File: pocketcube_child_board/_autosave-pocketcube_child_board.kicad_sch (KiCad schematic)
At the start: 7 parts, among them J1 M55-7102042R, U1 SI3477DV-T1-GE3

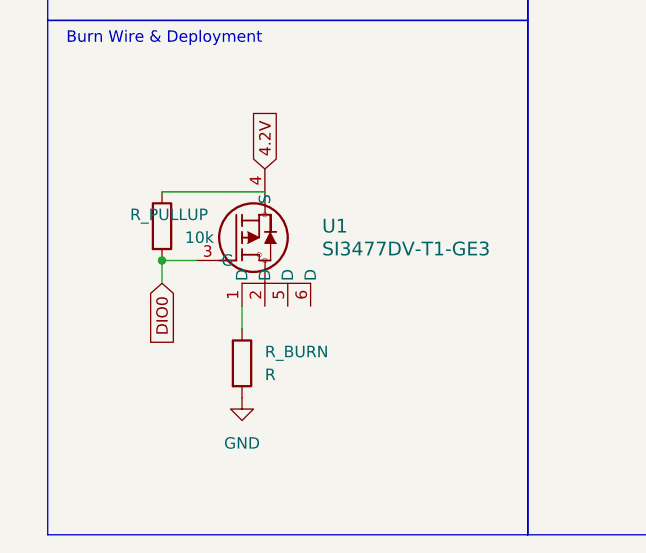
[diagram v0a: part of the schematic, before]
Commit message: implemented pmos
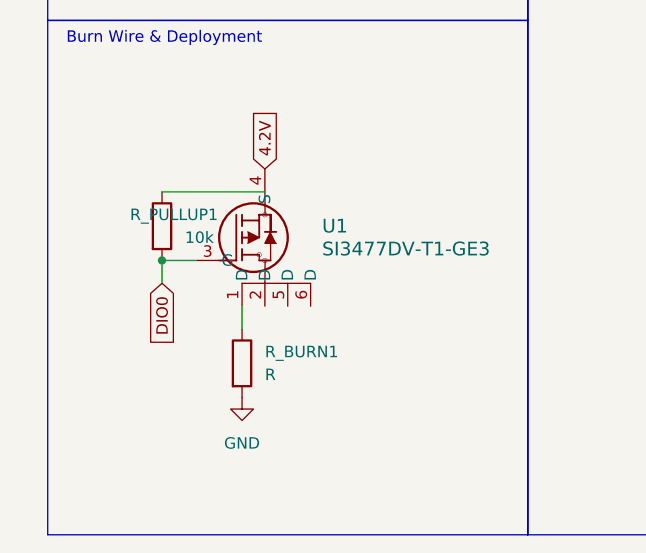
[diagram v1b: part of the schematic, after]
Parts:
- R_BURN1: renamed from R_BURN; footprint (none) -> Resistor_SMD:R_0201_0603Metric
- R_PULLUP1: renamed from R_PULLUP; footprint (none) -> Resistor_SMD:R_0201_0603Metric
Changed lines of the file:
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@@
 		(dnp no)
 		(fields_autoplaced yes)
-		(property "Reference" "R_BURN"
+		(property "Reference" "R_BURN1"
 			(at 36.83 101.5999 0)
 			(effects
@@
 			)
 		)
-		(property "Footprint" ""
+		(property "Footprint" "Resistor_SMD:R_0201_0603Metric"
 			(at 32.512 102.87 90)
 			(effects
@@
 			(project ""
 				(path "/a6e7c6fa-7853-41f6-bfd3-5d5ee6914f30"
-					(reference "R_BURN")
+					(reference "R_BURN1")
 					(unit 1)
 				)
@@
 		(on_board yes)
 		(dnp no)
-		(property "Reference" "R_PULLUP"
+		(property "Reference" "R_PULLUP1"
 			(at 21.844 86.36 0)
 			(effects
@@
 			)
 		)
-		(property "Footprint" ""
+		(property "Footprint" "Resistor_SMD:R_0201_0603Metric"
 			(at 23.622 87.63 90)
 			(effects
@@
 			(project ""
 				(path "/a6e7c6fa-7853-41f6-bfd3-5d5ee6914f30"
-					(reference "R_PULLUP")
-					(unit 1)
-				)
+					(reference "R_PULLUP1")
+					(unit 1)
+				)

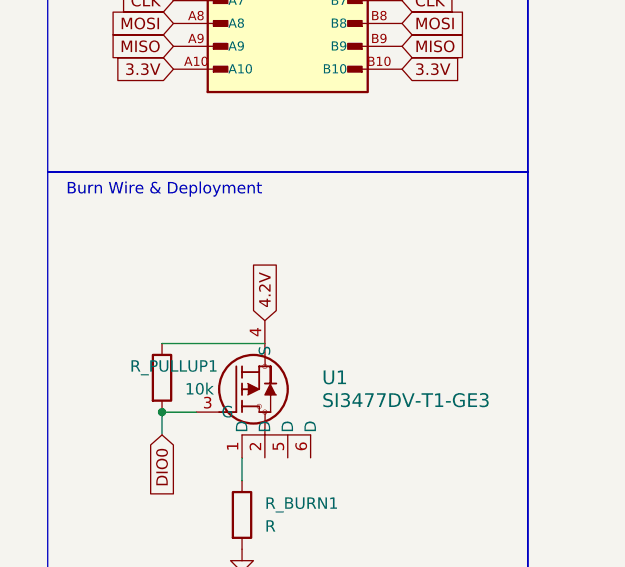
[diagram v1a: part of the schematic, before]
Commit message: pmos implementation
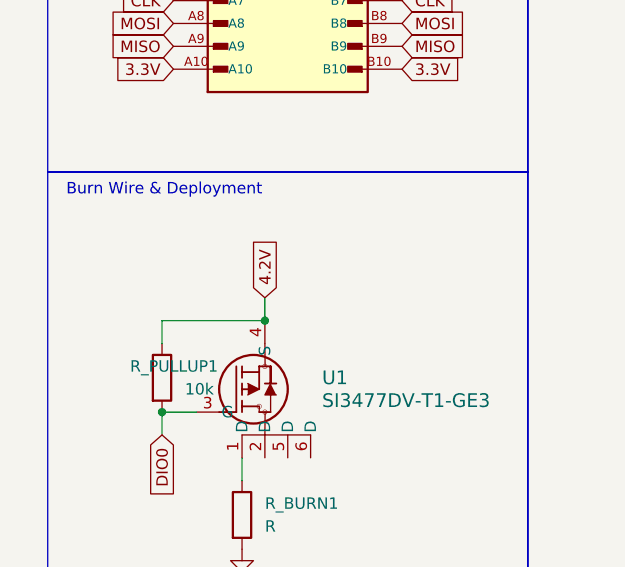
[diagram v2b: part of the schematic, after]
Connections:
- net 4.2V: now also R_PULLUP1.1
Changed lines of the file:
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@@
+	)
+	(junction
+		(at 36.83 81.28)
+		(diameter 0)
+		(color 0 0 0 0)
 	)
 	(junction
@@
 	(wire
 		(pts
+			(xy 25.4 81.28) (xy 25.4 83.82)
+		)
+		(stroke
+			(width 0)
+			(type default)
+		)
+	)
+	(wire
+		(pts
 			(xy 156.21 85.09) (xy 166.37 85.09)
 		)
@@
 	(wire
 		(pts
+			(xy 36.83 78.74) (xy 36.83 81.28)
+		)
+		(stroke
+			(width 0)
+			(type default)
+		)
+	)
+	(wire
+		(pts
 			(xy 124.46 36.83) (xy 124.46 39.37)
 		)
@@
 	(wire
 		(pts
+			(xy 25.4 81.28) (xy 36.83 81.28)
+		)
+		(stroke
+			(width 0)
+			(type default)
+		)
+	)
+	(wire
+		(pts
 			(xy 156.21 80.01) (xy 166.37 80.01)
 		)
@@
 	(wire
 		(pts
-			(xy 25.4 83.82) (xy 36.83 83.82)
-		)
-		(stroke
-			(width 0)
-			(type default)
-		)
-	)
-	(wire
-		(pts
 			(xy 166.37 80.01) (xy 166.37 82.55)
 		)
@@
 	(global_label "4.2V"
 		(shape input)
-		(at 36.83 81.28 90)
-		(fields_autoplaced yes)
-		(effects
-			(font
-				(size 1.27 1.27)
-			)
-			(justify left)
-		)
-		(property "Intersheetrefs" "${INTERSHEET_REFS}"
-			(at 36.83 74.1824 90)
-			(effects
-				(font
+		(at 36.83 78.74 90)
+		(fields_autoplaced yes)
+		(effects
+			(font
+				(size 1.27 1.27)
+			)
+			(justify left)
+		)
+		(property "Intersheetrefs" "${INTERSHEET_REFS}"
+			(at 36.83 71.6424 90)
+			(effects
+				(font

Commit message: Revert "pmos implementation"
This reverts commit 559285578e66f978812a0fb110e98bc36d41d9a4.
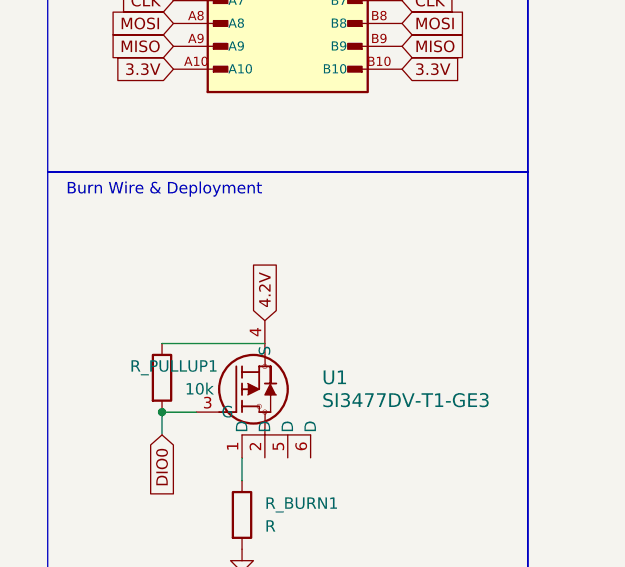
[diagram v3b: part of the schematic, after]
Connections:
- net 4.2V: no longer R_PULLUP1.1
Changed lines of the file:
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@@
-	)
-	(junction
-		(at 36.83 81.28)
-		(diameter 0)
-		(color 0 0 0 0)
 	)
 	(junction
@@
 	(wire
 		(pts
-			(xy 25.4 81.28) (xy 25.4 83.82)
-		)
-		(stroke
-			(width 0)
-			(type default)
-		)
-	)
-	(wire
-		(pts
 			(xy 156.21 85.09) (xy 166.37 85.09)
 		)
@@
 	(wire
 		(pts
-			(xy 36.83 78.74) (xy 36.83 81.28)
-		)
-		(stroke
-			(width 0)
-			(type default)
-		)
-	)
-	(wire
-		(pts
 			(xy 124.46 36.83) (xy 124.46 39.37)
 		)
@@
 	(wire
 		(pts
-			(xy 25.4 81.28) (xy 36.83 81.28)
-		)
-		(stroke
-			(width 0)
-			(type default)
-		)
-	)
-	(wire
-		(pts
 			(xy 156.21 80.01) (xy 166.37 80.01)
 		)
@@
 	(wire
 		(pts
+			(xy 25.4 83.82) (xy 36.83 83.82)
+		)
+		(stroke
+			(width 0)
+			(type default)
+		)
+	)
+	(wire
+		(pts
 			(xy 166.37 80.01) (xy 166.37 82.55)
 		)
@@
 	(global_label "4.2V"
 		(shape input)
-		(at 36.83 78.74 90)
-		(fields_autoplaced yes)
-		(effects
-			(font
-				(size 1.27 1.27)
-			)
-			(justify left)
-		)
-		(property "Intersheetrefs" "${INTERSHEET_REFS}"
-			(at 36.83 71.6424 90)
-			(effects
-				(font
+		(at 36.83 81.28 90)
+		(fields_autoplaced yes)
+		(effects
+			(font
+				(size 1.27 1.27)
+			)
+			(justify left)
+		)
+		(property "Intersheetrefs" "${INTERSHEET_REFS}"
+			(at 36.83 74.1824 90)
+			(effects
+				(font
